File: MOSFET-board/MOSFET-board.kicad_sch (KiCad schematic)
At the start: 6 parts, among them J1 PCIE-LP-01-01-F-DV-A-TR, J2 DB15_Female, J3 DB15_Female, J6 PCIE-164-02-X-D-TH, U11 PCF8575_Breakout

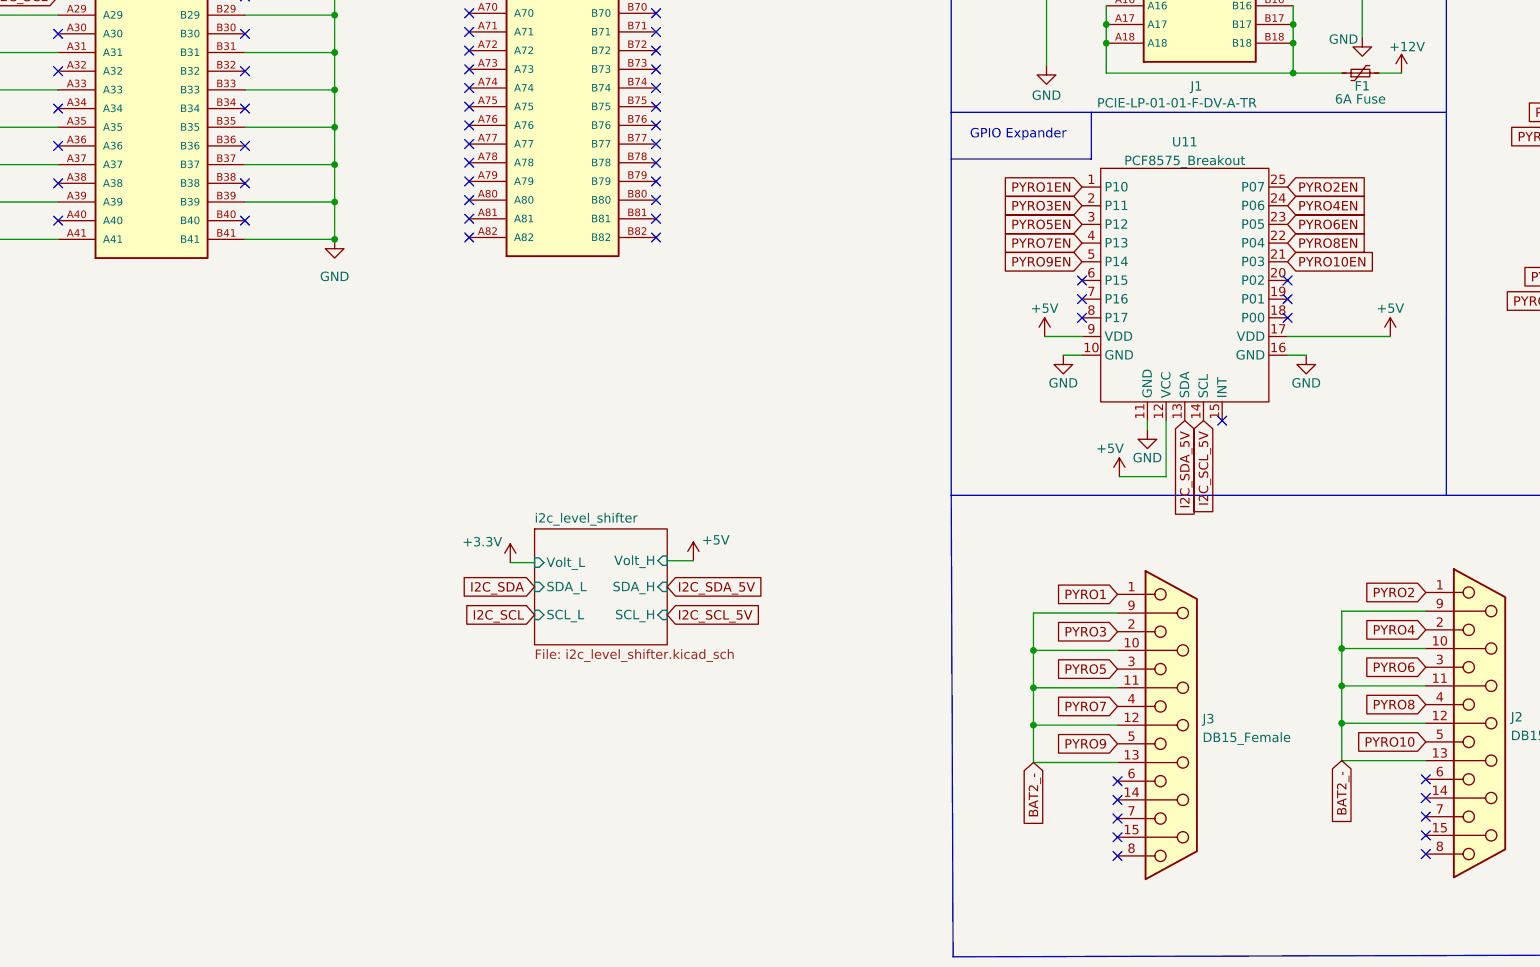
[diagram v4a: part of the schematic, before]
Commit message: Ironing out small details, changed pcf8575 to IC instead of breakout.
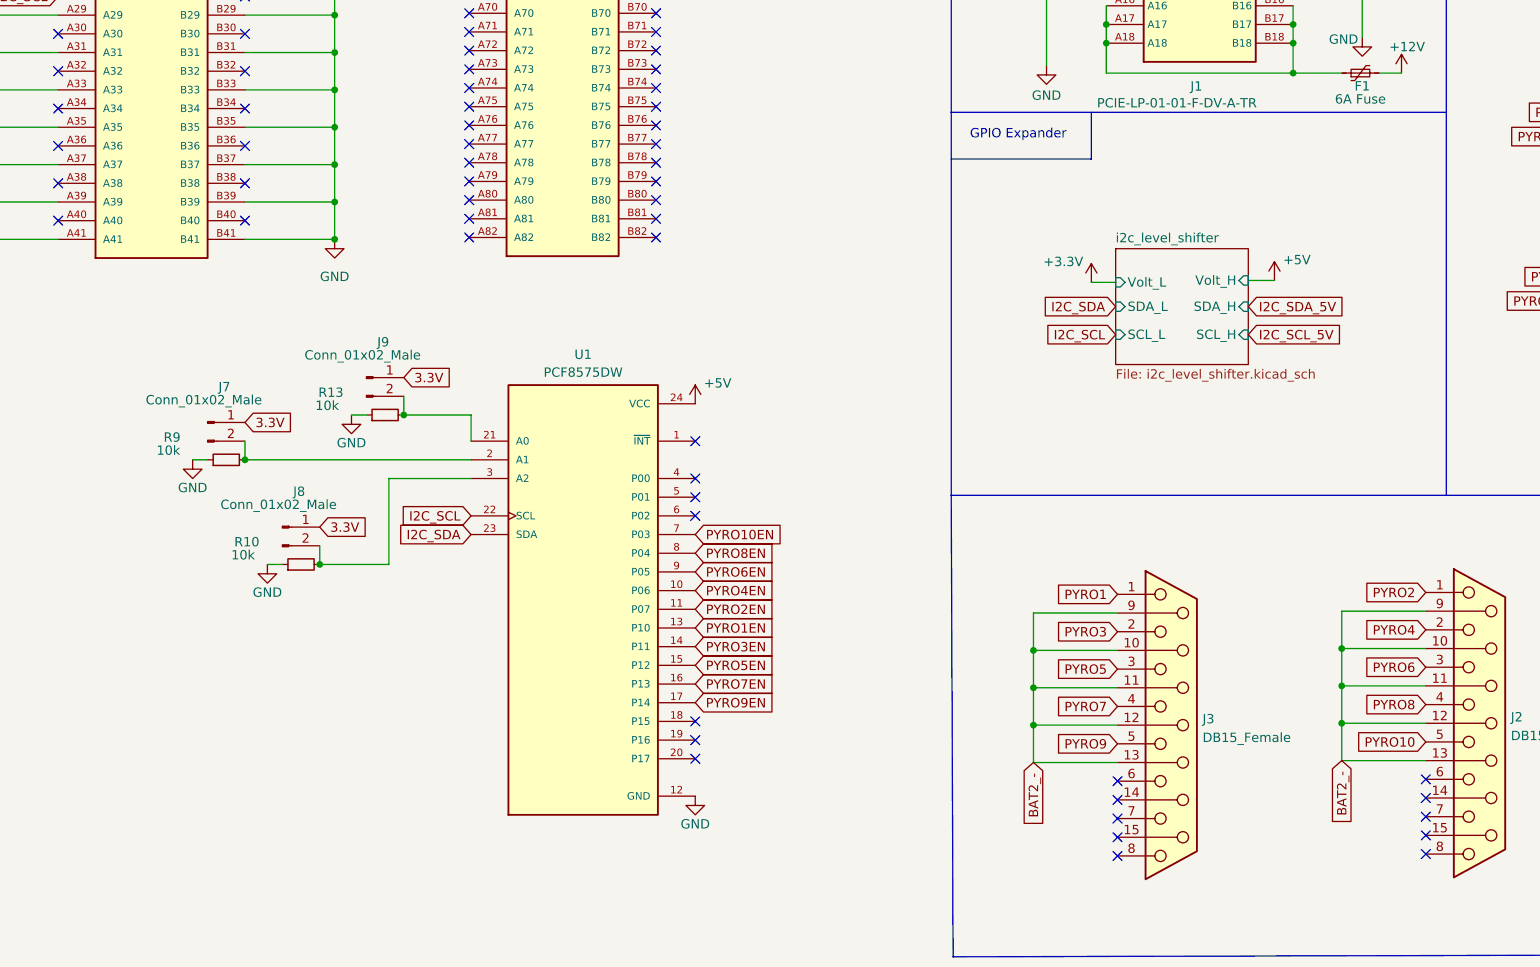
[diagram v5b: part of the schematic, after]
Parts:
- removed U11: PCF8575_Breakout, PCF8575_Breakout:PCF8575_Breakout, symbol PCF87575Breakout:PCF8575_Breakout
- added J7, J8, J9: Conn_01x02_Male, Connector_PinHeader_2.54mm:PinHeader_1x02_P2.54mm_Vertical, symbol Connector:Conn_01x02_Male
- added R10, R13, R9: 10k, Resistor_SMD:R_0603_1608Metric, symbol Device:R_Small
- added U1: PCF8575DW, PCF8575DW:SOIC127P1030X265-24N, symbol PCF8575DW:PCF8575DW
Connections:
- net +5V: now also U1.24 (VCC)
- net GND: now also R10.1, R13.1, R9.1, U1.12 (GND)
- net I2C_SCL: now also U1.22 (SCL)
- net I2C_SDA: now also U1.23 (SDA)
- net PYRO10EN: now also U1.7 (P03)
- net PYRO1EN: now also U1.13 (P10)
- net PYRO2EN: now also U1.11 (P07)
- net PYRO3EN: now also U1.14 (P11)
- net PYRO4EN: now also U1.10 (P06)
- net PYRO5EN: now also U1.15 (P12)
- net PYRO6EN: now also U1.9 (P05)
- net PYRO7EN: now also U1.16 (P13)
- net PYRO8EN: now also U1.8 (P04)
- net PYRO9EN: now also U1.17 (P14)
- new net: J7.2 (Pin_2), R9.2, U1.2 (A1)
- new net: J8.2 (Pin_2), R10.2, U1.3 (A2)
- new net: J9.2 (Pin_2), R13.2, U1.21 (A0)
- new net 3.3V: J7.1 (Pin_1), J8.1 (Pin_1), J9.1 (Pin_1)
